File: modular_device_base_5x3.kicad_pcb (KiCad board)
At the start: 2 copper layers, 135.9 x 67.3 mm, 48 parts, among them P1 PWR_JACK_2.5x5.5, P10 HEADER_01X02_SMD_RA, P11 HEADER_01X03_RA, P2 BNC_DOUBLE_RA, P3 HEADER_01X03_SMD_RA, P4 HEADER_01X02_SMD_RA, P5 HEADER_01X03_SMD_RA, P6 HEADER_01X02_SMD_RA, P7 HEADER_01X03_SMD_RA, P8 HEADER_01X02_SMD_RA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

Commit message: Progress towards v1.2.
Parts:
- added P12: HEADER_01X02_SMD_RA_UNSHR, footprints:Header_2_Pin_SMD_RA_UNSHR, B.Cu at (62.2, 123.8)
- added P13: HEADER_01X02_SMD_RA_UNSHR, footprints:Header_2_Pin_SMD_RA_UNSHR, B.Cu at (69.2, 69.2)
- turned SW1 to 0 degrees
- turned SW2 to 270 degrees
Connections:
- MH1 pad 1: (no net) -> Net-(MH1-Pad1)
- MH2 pad 1: (no net) -> Net-(MH2-Pad1)
- MH3 pad 1: (no net) -> Net-(MH3-Pad1)
- MH4 pad 1: (no net) -> Net-(MH4-Pad1)
- MH5 pad 1: (no net) -> Net-(MH5-Pad1)
- MH6 pad 1: (no net) -> Net-(MH6-Pad1)
- MH7 pad 1: (no net) -> Net-(MH7-Pad1)
- MH8 pad 1: (no net) -> Net-(MH8-Pad1)
- P11 pad 3: (no net) -> Net-(P11-Pad3)
- TEENSY1 pad 28: (no net) -> Net-(TEENSY1-Pad28)
- TEENSY1 pad 3: (no net) -> Net-(TEENSY1-Pad3)
- TEENSY1 pad 39: (no net) -> Net-(TEENSY1-Pad39)
- TEENSY1 pad 4: (no net) -> Net-(TEENSY1-Pad4)
- TEENSY1 pad PROG: (no net) -> Net-(TEENSY1-PadPROG)
- TEENSY1 pad RSET: (no net) -> Net-(TEENSY1-PadRSET)
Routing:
- net /LED_YEL: track 129.0 -> 84.7 mm, vias 1 -> 0
- net /RX2: track 115.5 -> 84.5 mm
- net GND: track 407.0 -> 391.2 mm, vias 2 -> 1
- net VDDA: track 30.5 -> 45.7 mm, vias 1 -> 2
- net VSSA: track 129.9 -> 140.9 mm, vias 1 -> 2
- net VEE: track 61.8 -> 52.6 mm
- net /LED_GRN: track 95.0 -> 86.0 mm
- net /RX1: track 116.6 -> 108.3 mm, vias 2 -> 1
- net /RX4: track 76.0 -> 84.2 mm, vias 2 -> 1
- net /TX4: track 71.9 -> 79.9 mm
- net /TX3: track 95.4 -> 100.7 mm, vias 2 -> 1
- net /D40: track 42.7 -> 37.5 mm, vias 1 -> 0
- net /TX1: track 105.7 -> 100.9 mm, vias 2 -> 1
- net /D49: track 38.5 -> 43.3 mm
- net /BTN_A: track 28.5 -> 32.5 mm
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- removed copper zone on B.Cu, net GND
- removed copper zone on F.Cu, net GND
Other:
- net class Default: clearance 0.2 -> 0
- rule trace_clearance: 0.2 -> 0
- board text added: "+12-42VDC"
- board text added: "2.5x5.5 Center + +12-42VDC"
- board text added: "DISABLE"
- board text added: "ENABLE"
- board text added: "Janelia Modular Device modular_device_base part_number: 1000 08/2017 ver 1.2 5x3"
- board text added: "RED LED"
- board text removed: "+9-42VDC"
- board text removed: "2.5x5.5 Center + +9-42VDC"
- board text removed: "Janelia Modular Device modular_device_base part_number: 1000 05/2017 ver 1.1 5x3"
- board text removed: "LED"
- board text removed: "OFF"
- board text removed: "ON"

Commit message: Finished v1.2.
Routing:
- net GND: track 391.2 -> 446.4 mm, vias 1 -> 3
- added copper zone on B.Cu, net GND
- added copper zone on F.Cu, net GND
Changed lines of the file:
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@@
     (thickness 1.6)
     (drawings 52)
-    (tracks 640)
+    (tracks 650)
     (zones 0)
     (modules 50)
@@
   (segment (start 180.0603 99.695) (end 178.5853 101.17) (width 1.2192) (layer F.Cu) (net 1))
   (segment (start 182.9562 99.695) (end 180.0603 99.695) (width 1.2192) (layer F.Cu) (net 1))
+  (segment (start 178.435 122.174) (end 178.435 128.905) (width 0.6096) (layer B.Cu) (net 2) (status 400000))
+  (via (at 153.67 103.505) (size 0.889) (drill 0.635) (layers F.Cu B.Cu) (net 2))
+  (segment (start 156.21 106.045) (end 153.67 103.505) (width 0.6096) (layer F.Cu) (net 2))
+  (segment (start 156.21 113.03) (end 156.21 106.045) (width 0.6096) (layer F.Cu) (net 2))
+  (segment (start 154.94 114.3) (end 156.21 113.03) (width 0.6096) (layer F.Cu) (net 2))
+  (via (at 154.94 114.3) (size 0.889) (drill 0.635) (layers F.Cu B.Cu) (net 2))
+  (segment (start 154.94 120.015) (end 154.94 114.3) (width 0.6096) (layer B.Cu) (net 2))
+  (segment (start 167.64 132.715) (end 154.94 120.015) (width 0.6096) (layer B.Cu) (net 2))
+  (segment (start 174.625 132.715) (end 167.64 132.715) (width 0.6096) (layer B.Cu) (net 2))
+  (segment (start 178.435 128.905) (end 174.625 132.715) (width 0.6096) (layer B.Cu) (net 2))
   (via (at 181.1046 83.998) (size 0.889) (drill 0.635) (layers F.Cu B.Cu) (net 2))
   (segment (start 182.4746 124.6993) (end 178.435 124.6993) (width 0.6096) (layer B.Cu) (net 2))
@@
   (segment (start 176.5788 110.49) (end 187.325 110.49) (width 0.6096) (layer B.Cu) (net 76))
   (segment (start 170.8638 116.205) (end 176.5788 110.49) (width 0.6096) (layer B.Cu) (net 76))
+  (zone (net 2) (net_name GND) (layer F.Cu) (hatch edge 0.508)
+    (connect_pads (clearance 0.2032))
+    (min_thickness 0.2032)
+    (fill yes (arc_segments 16) (thermal_gap 0.508) (thermal_bridge_width 0.508))
+    (polygon
+      (pts
+        (xy 58.42 65.405) (xy 58.42 133.985) (xy 195.58 133.985) (xy 195.58 65.405)
+      )
+    )
+  )
+  (zone (net 2) (net_name GND) (layer B.Cu) (hatch edge 0.508)
+    (connect_pads (clearance 0.2032))
+    (min_thickness 0.2032)
+    (fill yes (arc_segments 16) (thermal_gap 0.508) (thermal_bridge_width 0.508))
+    (polygon
+      (pts
+        (xy 57.785 64.77) (xy 57.785 134.62) (xy 196.215 134.62) (xy 196.215 64.77)
+      )
+    )
+  )
 )

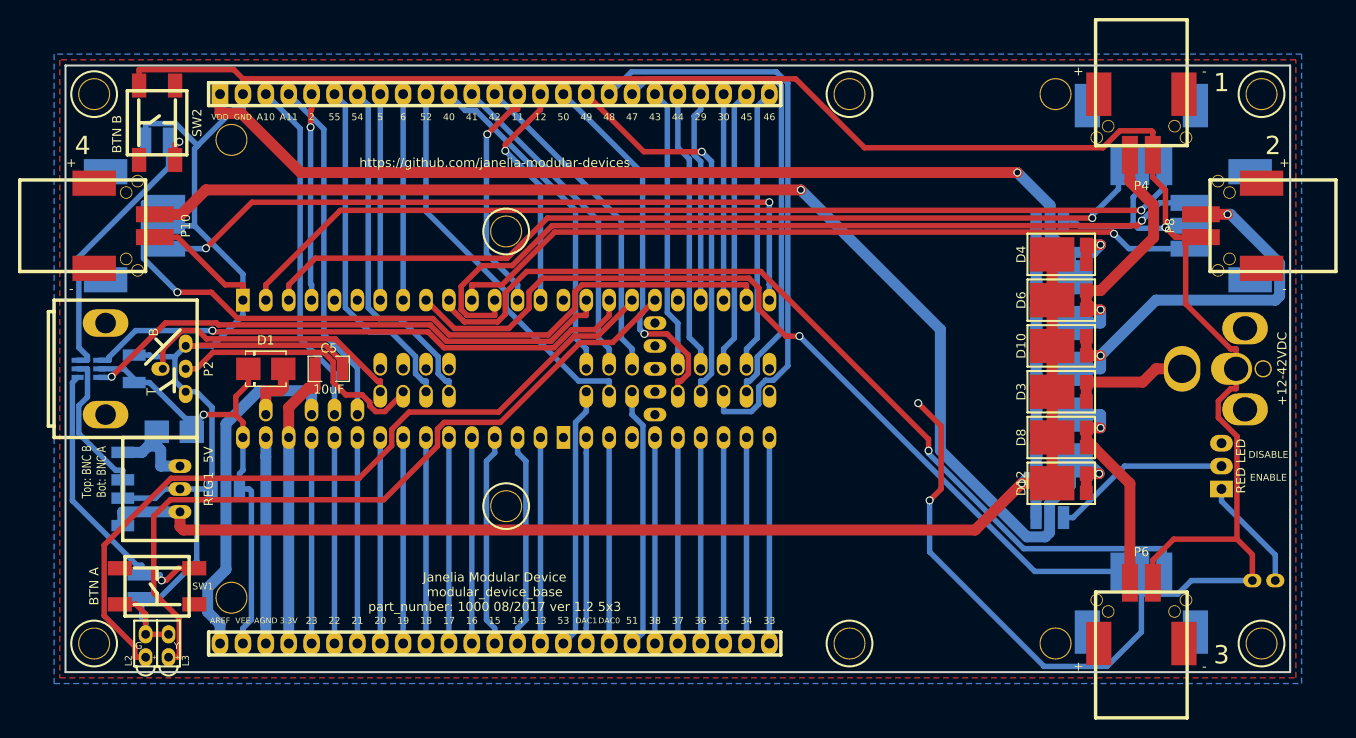
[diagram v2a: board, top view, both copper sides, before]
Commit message: Add schematics
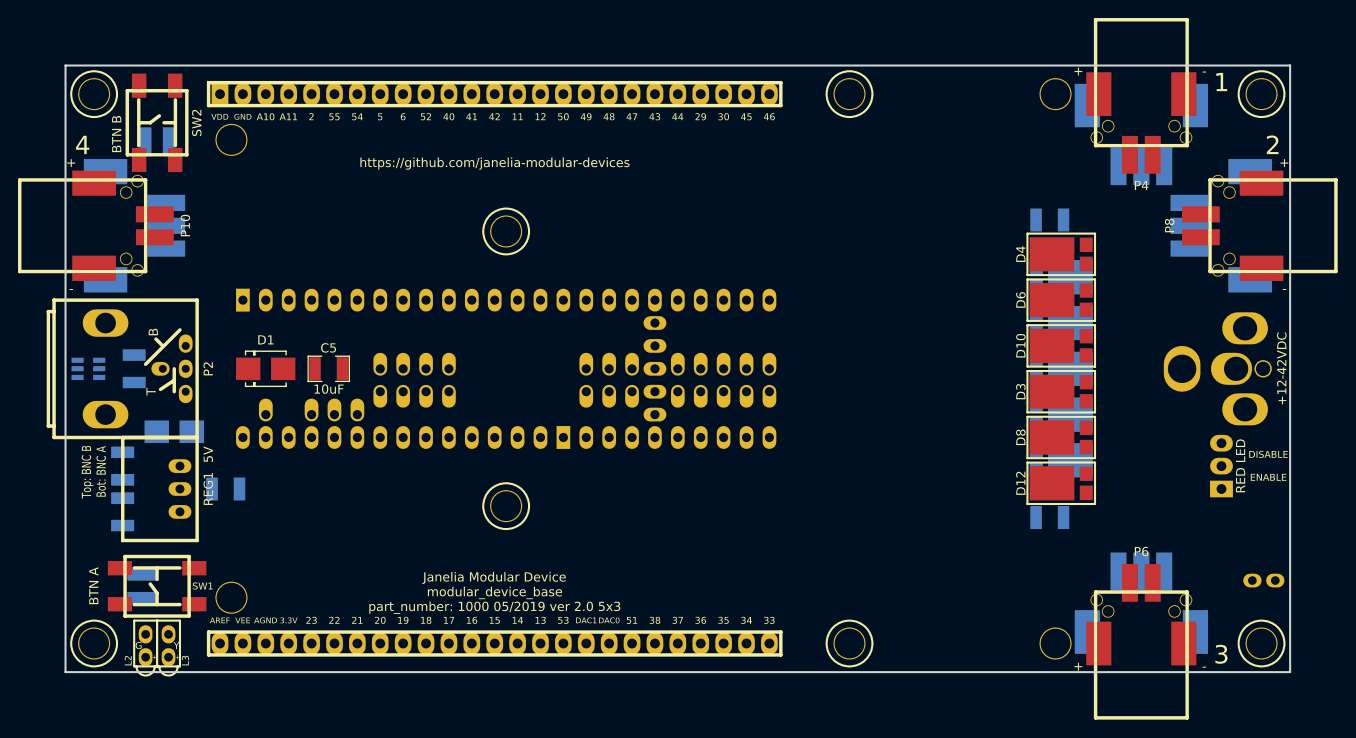
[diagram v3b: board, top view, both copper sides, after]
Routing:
- net GND: track 446.4 -> 0.00 mm, vias 3 -> 0
- net VPP: track 168.8 -> 0.00 mm, vias 1 -> 0
- net VSSA: track 140.9 -> 0.00 mm, vias 2 -> 0
- net VDD: track 115.5 -> 0.00 mm, vias 2 -> 0
- net /RX1: track 108.3 -> 0.00 mm, vias 1 -> 0
- net /TX1: track 100.9 -> 0.00 mm, vias 1 -> 0
- net /TX3: track 100.7 -> 0.00 mm, vias 1 -> 0
- net /RX3: track 96.4 -> 0.00 mm, vias 1 -> 0
- net /TX2: track 92.9 -> 0.00 mm, vias 1 -> 0
- net /LED_GRN: track 86.0 -> 0.00 mm
- net /LED_YEL: track 84.7 -> 0.00 mm
- net /RX2: track 84.5 -> 0.00 mm, vias 1 -> 0
- net /RX4: track 84.2 -> 0.00 mm, vias 1 -> 0
- net /TX4: track 79.9 -> 0.00 mm, vias 2 -> 0
- net /D48: track 65.3 -> 0.00 mm
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- removed copper zone on B.Cu, net GND
- removed copper zone on F.Cu, net GND
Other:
- board text added: "Janelia Modular Device modular_device_base part_number: 1000 05/2019 ver 2.0 5x3"
- board text removed: "Janelia Modular Device modular_device_base part_number: 1000 08/2017 ver 1.2 5x3"
